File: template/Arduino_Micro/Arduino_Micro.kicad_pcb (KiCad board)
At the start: 2 copper layers, 17.8 x 48.3 mm, 6 parts, among them P1 Digital, P2 Analog, P3 CONN_01X01, P4 CONN_01X01, P5 CONN_01X01, P6 CONN_01X01

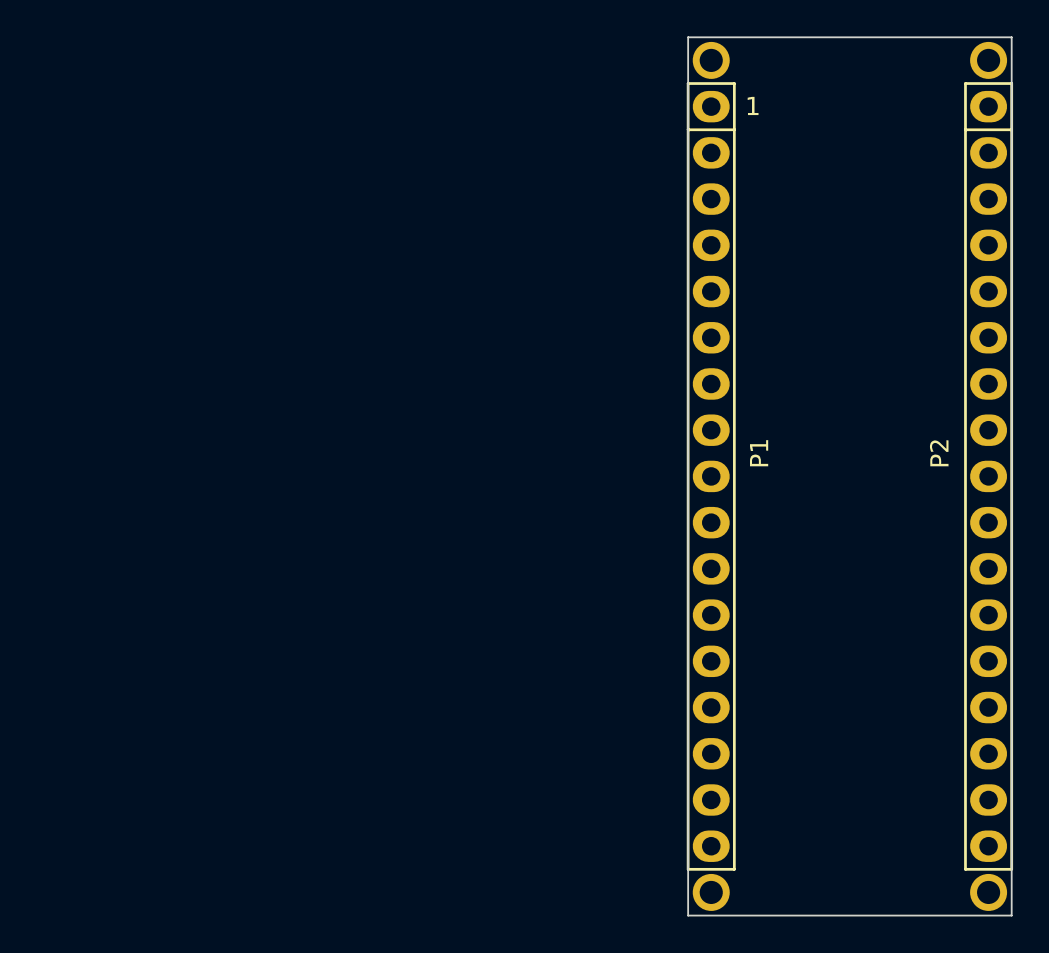
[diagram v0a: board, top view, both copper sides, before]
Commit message: fix: change original libs; add: new components
- Fix LIS3DH pins positions;
- Add ATmega164P symbol;
- Add 3D model to the L_Wuerth_HCM-7050;
- Add parameters for R_RES (Assembly...).
- Add parameters for R_RES and C_CAP;
- Fix SOIC-8 package 3D model;
- Add new parameters for many symbols;
- Change text height from 70 mil to 50 mil;
- Add solder mask expansion for 2-contact jumpers;
- Change thermopad vias of QFN-20-1EP_3x3mm_P0.45mm_EP1.6x1.6mm_ThermalVias;
- Add D_SMAF footprint;
- Fillet silk for C_1206;
-Rectangle silk for R_1206;
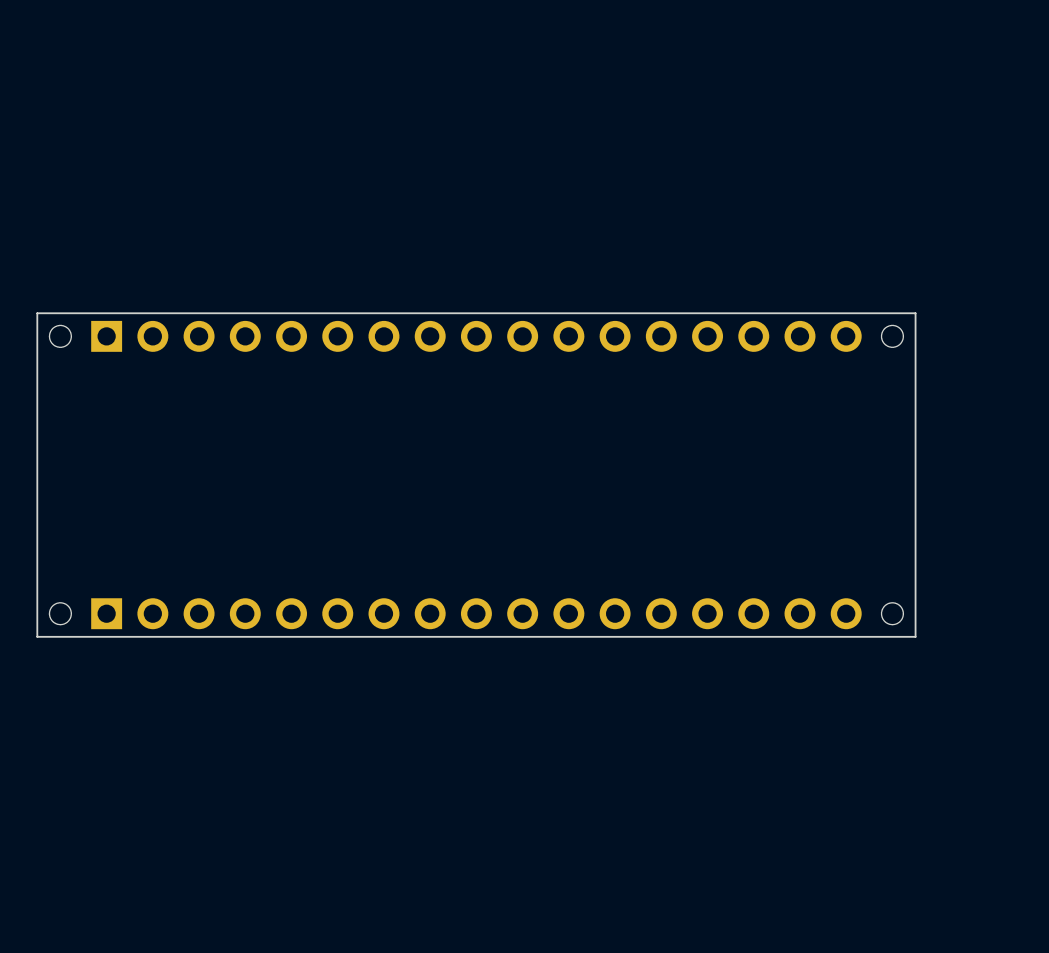
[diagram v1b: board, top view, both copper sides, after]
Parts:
- removed P3, P4, P5, P6: CONN_01X01, Socket_Arduino_Micro:1pin_Micro
- added MH1: MountingHole_1.2mm, Arduino_MountingHole:MountingHole_1.2mm, F.Cu at (101.3, 98.7)
- added MH2: MountingHole_1.2mm, Arduino_MountingHole:MountingHole_1.2mm, F.Cu at (101.3, 83.5)
- added MH3: MountingHole_1.2mm, Arduino_MountingHole:MountingHole_1.2mm, F.Cu at (147.0, 83.5)
- added MH4: MountingHole_1.2mm, Arduino_MountingHole:MountingHole_1.2mm, F.Cu at (147.0, 98.7)
- J1: renamed from P1; value Digital -> Analog; footprint Socket_Arduino_Micro:Socket_Strip_Arduino_1x17 -> Connector_PinHeader_2.54mm:PinHeader_1x17_P2.54mm_Vertical; moved to B.Cu
- J2: renamed from P2; value Analog -> Digital; footprint Socket_Arduino_Micro:Socket_Strip_Arduino_1x17 -> Connector_PinHeader_2.54mm:PinHeader_1x17_P2.54mm_Vertical; moved to B.Cu
- moved J2 50.1 mm to (103.8, 83.5)
- moved J1 43.4 mm to (103.8, 98.7)
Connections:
- net /10(A10) renamed VCC
- net /11(**) renamed /D14/MISO
- net /12(A11) renamed /D15/SCK
- net /13(**) renamed /D16/MOSI
- net /MISO renamed /*D11
- net /MOSI renamed /*D13
- net /SCK renamed /D12
- net /Vin renamed /*D10
- net Net-(P2-Pad7) renamed /*D6
- net Net-(P2-Pad8) renamed /*D5
- J1 pad 10: /5(**) -> unconnected-(J1-Pad10)
- J1 pad 11: /6(**/A7) -> unconnected-(J1-Pad11)
- J1 pad 12: /7 -> +5V
- J1 pad 13: /8(A8) -> /~{RESET}
- J1 pad 14: /9(**/A9) -> GND
- J1 pad 2: /SS -> +3V3
- J1 pad 3: /1(Tx1) -> /AREF
- J1 pad 4: /0(Rx1) -> /A0
- J1 pad 5: /Reset -> /A1
- J1 pad 6: GND -> /A2
- J1 pad 7: /2(SDA) -> /A3
- J1 pad 8: /3(**/SCL) -> /A4
- J1 pad 9: /4(A6) -> /A5
- J2 pad 10: /A4 -> /*D3/SCL
- J2 pad 11: /A3 -> /D2/SDA
- J2 pad 12: /A2 -> GND
- J2 pad 13: /A1 -> /~{RESET}
- J2 pad 14: /A0 -> /D0/RX
- J2 pad 15: /AREF -> /D1/TX
- J2 pad 16: +3V3 -> /D17/SS
- J2 pad 4: GND -> /*D9
- J2 pad 5: /Reset -> /D8
- J2 pad 6: +5V -> /D7
- J2 pad 9: /A5 -> /D4
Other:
- board size 17.8 x 48.3 mm -> 48.3 x 17.8 mm
- board text added: "ICSP"
- board text added: "USB Micro-B"
- board text removed: "1"
